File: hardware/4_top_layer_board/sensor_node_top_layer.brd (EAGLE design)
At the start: 27.9 x 30.5 mm, 8 parts

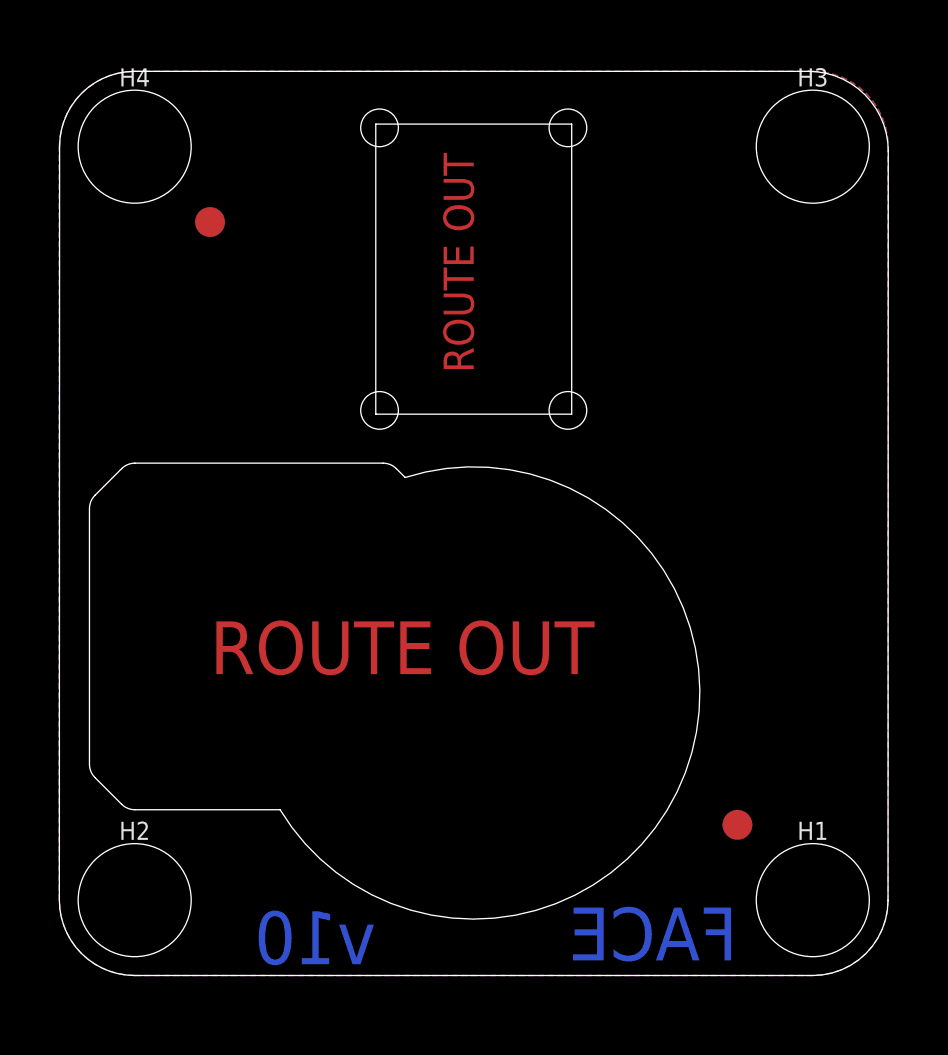
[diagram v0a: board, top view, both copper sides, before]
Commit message: increase width of shield
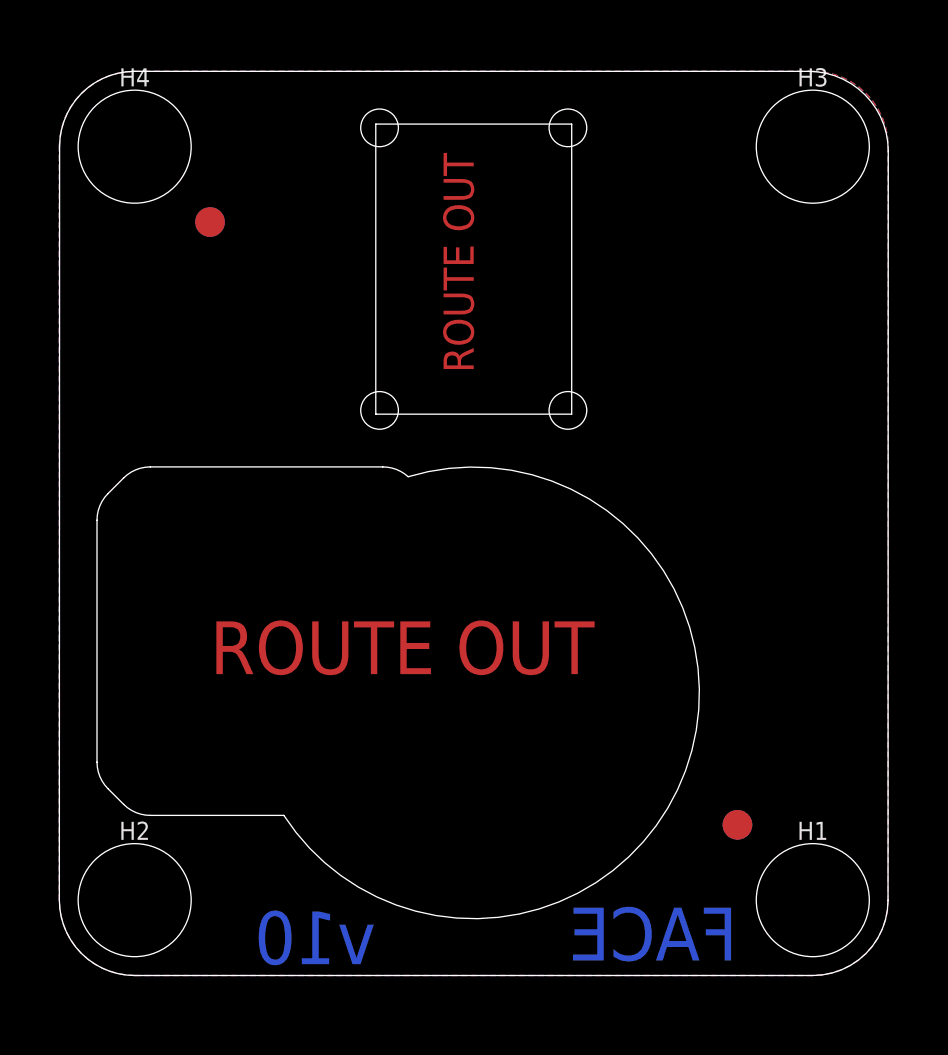
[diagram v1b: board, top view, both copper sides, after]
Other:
- outline, holes or cut-outs redrawn
